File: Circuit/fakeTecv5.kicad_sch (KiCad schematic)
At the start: 74 parts, among them J1 EXTRA, J11 FET1 3,3, J12 FET2 3,3, J13 FET3 3,3, J14 GPS Pins, J16 Encoder Pads, J37 SCL, J38 JST-SH-4, J39 SDA, J40 3.3V, J41 GND, J42 FET1, J43 FET2, J44 FET3, J45 GND, J46 Conn_01x02_Socket, J47 GND, J48 GND, J49 GND, J5 I2C Oled screen, J50 JST-SH-4, J6 FET1 Drain, J7 FET2 Drain, J8 FET3 Drain, J9 Molex PicoBlade 0532610271, M1 ERM Motor, Q1 AO3400A, Q2 AO3400A, Q3 AO3400A, SW1 Reset, SW2 SW_Push, SW3 RotaryEncoder_Switch, U1 XB8089D0, U2 HT-RA62, U3 nice!nano v2

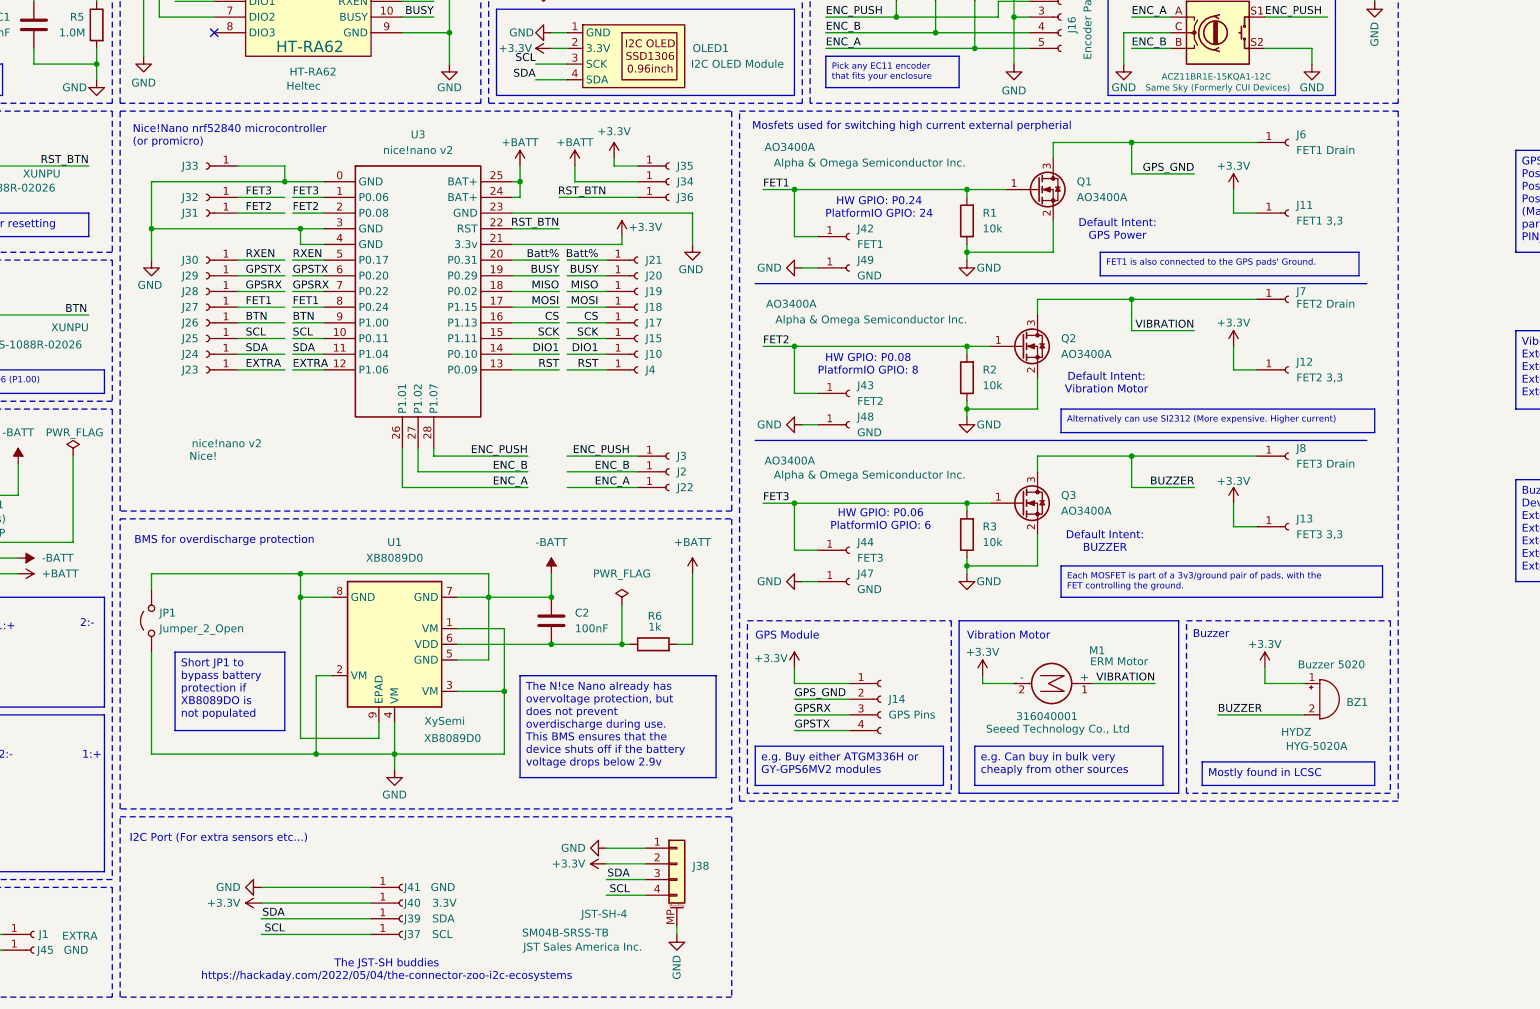
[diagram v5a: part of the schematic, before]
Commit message: hw: Add GPS slot and mark as Rev5.2
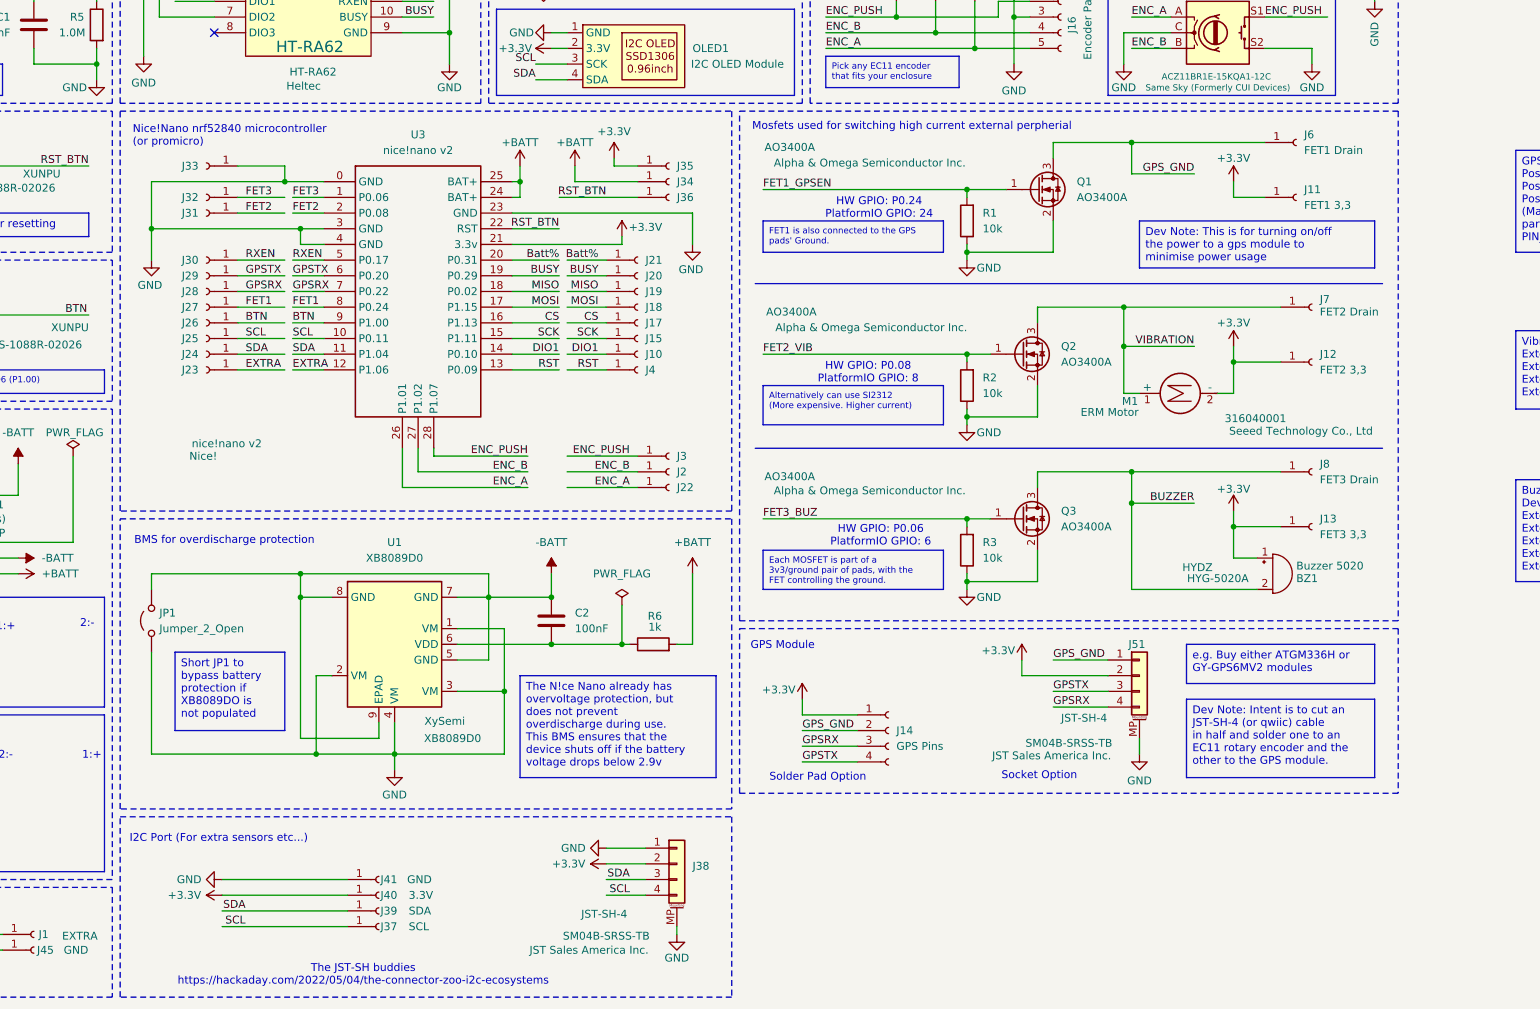
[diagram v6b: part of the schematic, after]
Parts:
- removed J42: FET1, faketec:SMD_PAD_1x01, symbol Connector:Conn_01x01_Socket
- removed J43: FET2, faketec:SMD_PAD_1x01, symbol Connector:Conn_01x01_Socket
- removed J44: FET3, faketec:SMD_PAD_1x01, symbol Connector:Conn_01x01_Socket
- removed J47, J48, J49: GND, faketec:SMD_PAD_1x01, symbol Connector:Conn_01x01_Socket
- added J51: JST-SH-4, Connector_JST:JST_SH_SM04B-SRSS-TB_1x04-1MP_P1.00mm_Horizontal, symbol Connector_Generic_MountingPin:Conn_01x04_MountingPin
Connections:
- net +3.3V: now also J51.2 (Pin_2)
- net FET1: no longer Q1.1 (G), R1.2
- net FET2: no longer Q2.1 (G), R2.2
- net FET3: no longer Q3.1 (G), R3.2
- net GND: now also J51.MP (MountPin)
- net GPSRX: now also J51.4 (Pin_4)
- net GPSTX: now also J51.3 (Pin_3)
- net GPS_GND: now also J51.1 (Pin_1)
- new net FET1_GPSEN: Q1.1 (G), R1.2
- new net FET2_VIB: Q2.1 (G), R2.2
- new net FET3_BUZ: Q3.1 (G), R3.2
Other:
- note added: "Socket Option"
- note added: "Solder Pad Option"
- note removed: "Buzzer"
- note removed: "Default Intent: BUZZER"
- note removed: "Default Intent: GPS Power"
- note removed: "Default Intent: Vibration Motor"
- note removed: "Vibration Motor"
- moved on the sheet: BZ1, J11, J12, J13, J14, J37, J39, J40, J41, J6, J7, J8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
